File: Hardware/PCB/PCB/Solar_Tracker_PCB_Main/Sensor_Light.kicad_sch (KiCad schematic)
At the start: 4 parts, among them IC2 OPT3001DNPRQ1

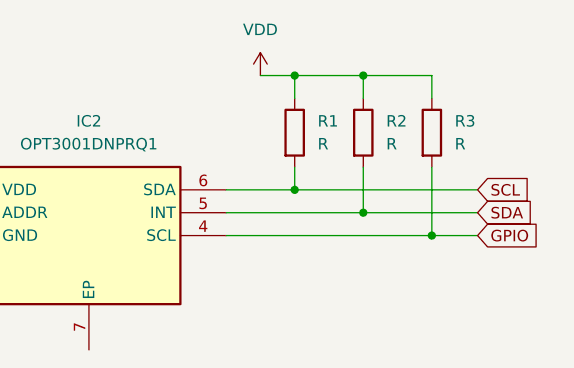
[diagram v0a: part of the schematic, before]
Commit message: Agregue el sensor
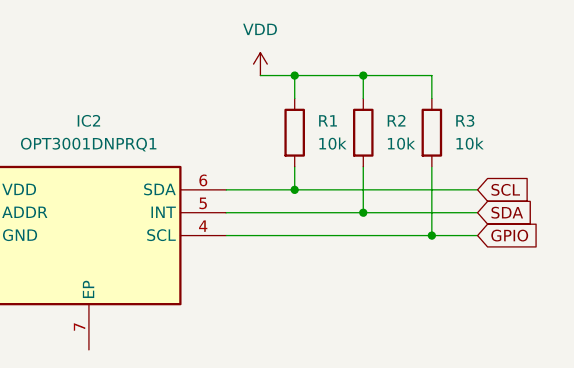
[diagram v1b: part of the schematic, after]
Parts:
- R1, R2, R3: value R -> 10k
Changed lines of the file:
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@@
 			)
 		)
-		(property "Value" "R"
+		(property "Value" "10k"
 			(at 172.72 74.9299 0)
 			(effects
@@
 			)
 		)
-		(property "Value" "R"
+		(property "Value" "10k"
 			(at 165.1 74.9299 0)
 			(effects
@@
 			)
 		)
-		(property "Value" "R"
+		(property "Value" "10k"
 			(at 157.48 74.9299 0)
 			(effects

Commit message: pcb
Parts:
- added IC3, IC4, IC5: OPT3001DNPRQ1, OPT3001DNDPRQ1:SON65P200X200X65-7N-D, symbol OPT3001DNPRQ1:OPT3001DNPRQ1
- added R10, R11, R12, R4, R5, R6, R7, R8, R9: 10k, symbol Device:R
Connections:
- net GND: now also IC3.2 (ADDR), IC3.3 (GND), IC4.2 (ADDR), IC4.3 (GND), IC5.2 (ADDR), IC5.3 (GND)
- net GPIO: now also IC3.4 (SCL), IC4.4 (SCL), IC5.4 (SCL), R12.2, R6.2, R9.2
- net SCL: now also IC3.6 (SDA), IC4.6 (SDA), IC5.6 (SDA), R10.2, R4.2, R7.2
- net SDA: now also IC3.5 (INT), IC4.5 (INT), IC5.5 (INT), R11.2, R5.2, R8.2
- net VDD: now also IC3.1 (VDD), IC4.1 (VDD), IC5.1 (VDD), R10.1, R11.1, R12.1, R4.1, R5.1, R6.1, R7.1, R8.1, R9.1
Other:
- moved on the sheet: IC2, R1, R2, R3
